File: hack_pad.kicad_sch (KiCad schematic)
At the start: 407 parts, among them J1 Barrel_Jack_Switch, Q1 IRLZ44N, Q2 IRF9540N, Q3 IRF9540N, Q4 IRLZ44N, SW1 SW_Push, SW10 SW_Push, SW100 SW_Push, SW11 SW_Push, SW12 SW_Push, SW13 SW_Push, SW14 SW_Push, SW15 SW_Push, SW16 SW_Push, SW17 SW_Push, SW18 SW_Push, SW19 SW_Push, SW2 SW_Push, SW20 SW_Push, SW21 SW_Push, SW22 SW_Push, SW23 SW_Push, SW24 SW_Push, SW25 SW_Push, SW26 SW_Push, SW27 SW_Push, SW28 SW_Push, SW29 SW_Push, SW3 SW_Push, SW30 SW_Push, SW31 SW_Push, SW32 SW_Push, SW33 SW_Push, SW34 SW_Push, SW35 SW_Push, SW36 SW_Push, SW37 SW_Push, SW38 SW_Push, SW39 SW_Push, SW4 SW_Push, SW40 SW_Push, SW41 SW_Push, SW42 SW_Push, SW43 SW_Push, SW44 SW_Push, SW45 SW_Push, SW46 SW_Push, SW47 SW_Push, SW48 SW_Push, SW49 SW_Push, SW5 SW_Push, SW50 SW_Push, SW51 SW_Push, SW52 SW_Push, SW53 SW_Push, SW54 SW_Push, SW55 SW_Push, SW56 SW_Push, SW57 SW_Push, SW58 SW_Push, SW59 SW_Push, SW6 SW_Push, SW60 SW_Push, SW61 SW_Push, SW62 SW_Push, SW63 SW_Push, SW64 SW_Push, SW65 SW_Push, SW66 SW_Push, SW67 SW_Push, SW68 SW_Push, SW69 SW_Push, SW7 SW_Push, SW70 SW_Push, SW71 SW_Push, SW72 SW_Push, SW73 SW_Push, SW74 SW_Push, SW75 SW_Push, SW76 SW_Push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

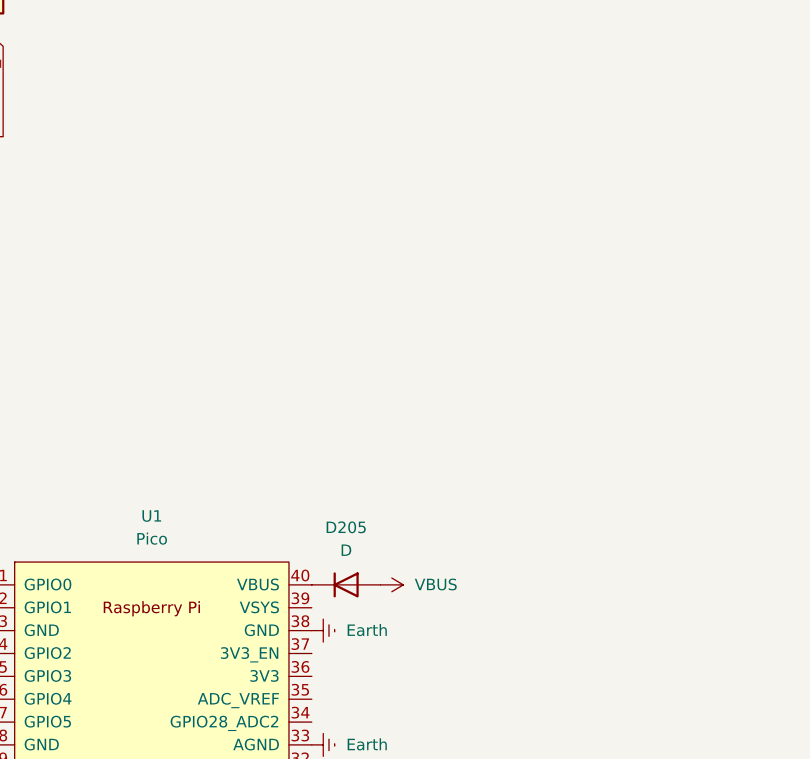
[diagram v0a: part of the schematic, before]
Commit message: Add initial journal entries and PCB lock file
- Created a journal.md to document the progress of the first PCB project, including details about the design, components, and layout.
- Added images of the PCB layout and components such as the RPI Pico and OLED.
- Introduced a lock file for the schematic to track user information.
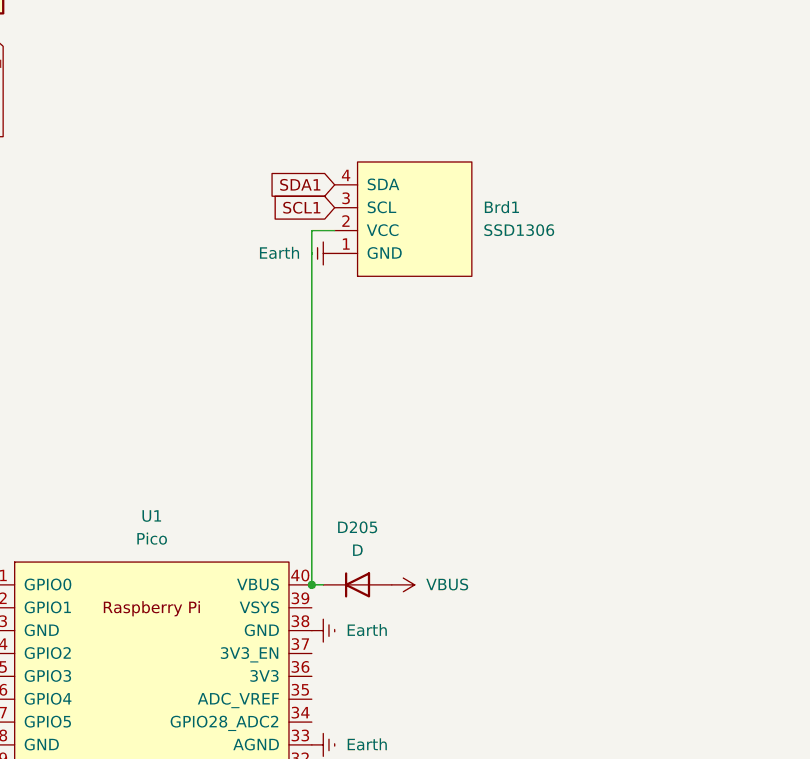
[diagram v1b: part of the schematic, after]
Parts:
- added Brd1: SSD1306, Display:OLED-128O064D, symbol SSD1306-0.91_OLED:SSD1306
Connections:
- net Earth: now also Brd1.1 (GND)
- net SCL1: now also Brd1.3 (SCL)
- net SDA1: now also Brd1.4 (SDA)
- net at D205.1 (K), U1.40 (VBUS): now also Brd1.2 (VCC)
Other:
- moved on the sheet: D205
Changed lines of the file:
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@@
 	)
 	(junction
+		(at 422.91 99.06)
+		(diameter 0)
+		(color 0 0 0 0)
+	)
+	(junction
 		(at 294.64 172.72)
 		(diameter 0)
@@
 	(wire
 		(pts
+			(xy 422.91 59.69) (xy 425.45 59.69)
+		)
+		(stroke
+			(width 0)
+			(type default)
+		)
+	)
+	(wire
+		(pts
 			(xy 76.2 190.5) (xy 91.44 190.5)
 		)
@@
 	(wire
 		(pts
+			(xy 424.18 99.06) (xy 422.91 99.06)
+		)
+		(stroke
+			(width 0)
+			(type default)
+		)
+	)
+	(wire
+		(pts
 			(xy 152.4 172.72) (xy 167.64 172.72)
 		)
@@
 	(wire
 		(pts
+			(xy 422.91 99.06) (xy 422.91 59.69)
+		)
+		(stroke
+			(width 0)
+			(type default)
+		)
+	)
+	(wire
+		(pts
 			(xy 157.48 111.76) (xy 157.48 129.54)
 		)
@@
 		)
 	)
+	(global_label "SCL1"
+		(shape input)
+		(at 425.45 57.15 180)
+		(fields_autoplaced yes)
+		(effects
+			(font
+				(size 1.27 1.27)
+			)
+			(justify right)
+		)
+		(property "Intersheetrefs" "${INTERSHEET_REFS}"
+			(at 417.7477 57.15 0)
+			(effects
+				(font
+					(size 1.27 1.27)
+				)
+				(justify right)
+				(hide yes)
+			)
+		)
+	)
+	(global_label "SDA1"
+		(shape input)
+		(at 425.45 54.61 180)
+		(fields_autoplaced yes)
+		(effects
+			(font
+				(size 1.27 1.27)
+			)
+			(justify right)
+		)
+		(property "Intersheetrefs" "${INTERSHEET_REFS}"
+			(at 417.6872 54.61 0)
+			(effects
+				(font
+					(size 1.27 1.27)
+				)
+				(justify right)
+				(hide yes)
+			)
+		)
+	)
 	(global_label "SDA1"
 		(shape input)
@@
 	(symbol
 		(lib_id "Device:D")
-		(at 426.72 99.06 0)
+		(at 427.99 99.06 0)
 		(unit 1)
 		(exclude_from_sim no)
@@
 		(fields_autoplaced yes)
 		(property "Reference" "D205"
-			(at 426.72 92.71 0)
+			(at 427.99 92.71 0)
 			(effects
 				(font
@@
 		)
 		(property "Value" "D"
-			(at 426.72 95.25 0)
+			(at 427.99 95.25 0)
 			(effects
 				(font
@@
 		)
 		(property "Footprint" "Diode_SMD:D_SMA_Handsoldering"
-			(at 426.72 99.06 0)
+			(at 427.99 99.06 0)
 			(effects
 				(font
@@
 		)
 		(property "Datasheet" "~"
-			(at 426.72 99.06 0)
+			(at 427.99 99.06 0)
 			(effects
 				(font
@@
 		)
 		(property "Description" "Diode"
-			(at 426.72 99.06 0)
+			(at 427.99 99.06 0)
 			(effects
 				(font
@@
 		)
 		(property "Sim.Device" "D"
-			(at 426.72 99.06 0)
+			(at 427.99 99.06 0)
 			(effects
 				(font
@@
 		)
 		(property "Sim.Pins" "1=K 2=A"
-			(at 426.72 99.06 0)
+			(at 427.99 99.06 0)
 			(effects
 				(font
@@
 	)
 	(symbol
+		(lib_id "SSD1306-0.91_OLED:SSD1306")
+		(at 434.34 58.42 90)
+		(unit 1)
+		(exclude_from_sim no)
+		(in_bom yes)
+		(on_board yes)
+		(dnp no)
+		(fields_autoplaced yes)
+		(property "Reference" "Brd1"
+			(at 441.96 57.1499 90)
+			(effects
+				(font
+					(size 1.27 1.27)
+				)
+				(justify right)
+			)
+		)
+		(property "Value" "SSD1306"
+			(at 441.96 59.6899 90)
+			(effects
+				(font
+					(size 1.27 1.27)
+				)
+				(justify right)
+			)
+		)
+		(property "Footprint" "Display:OLED-128O064D"
+			(at 427.99 58.42 0)
+			(effects
+				(font
+					(size 1.27 1.27)
+				)
+				(hide yes)
+			)
+		)
+		(property "Datasheet" ""
+			(at 427.99 58.42 0)
+			(effects
+				(font
+					(size 1.27 1.27)
+				)
+				(hide yes)
+			)
+		)
+		(property "Description" "SSD1306 OLED"
+			(at 434.34 58.42 0)
+			(effects
+				(font
+					(size 1.27 1.27)
+				)
+				(hide yes)
+			)
+		)
+		(pin "2"
+		)
+		(pin "3"
+		)
+		(pin "4"
+		)
+		(pin "1"
+		)
+		(instances
+			(project ""
+				(path "/d4b0ca01-3fca-43e7-acf5-9c62f788d69d"
+					(reference "Brd1")
+					(unit 1)
+				)
+			)
+		)
+	)
+	(symbol
 		(lib_id "LED:SK6812MINI")
 		(at 237.49 210.82 0)
@@
 	(symbol
 		(lib_id "power:Earth")
+		(at 425.45 62.23 270)
+		(unit 1)
+		(exclude_from_sim no)
+		(in_bom yes)
+		(on_board yes)
+		(dnp no)
+		(fields_autoplaced yes)
+		(property "Reference" "#PWR0212"
+			(at 419.1 62.23 0)
+			(effects
+				(font
+					(size 1.27 1.27)
+				)
+				(hide yes)
+			)
+		)
+		(property "Value" "Earth"
+			(at 421.64 62.2299 90)
+			(effects
+				(font
+					(size 1.27 1.27)
+				)
+				(justify right)
+			)
+		)
+		(property "Footprint" ""
+			(at 425.45 62.23 0)
+			(effects
+				(font
+					(size 1.27 1.27)
+				)
+				(hide yes)
+			)
+		)
+		(property "Datasheet" "~"
+			(at 425.45 62.23 0)
+			(effects
+				(font
+					(size 1.27 1.27)
+				)
+				(hide yes)
+			)
+		)
+		(property "Description" "Power symbol creates a global label with name \"Earth\""
+			(at 425.45 62.23 0)
+			(effects
+				(font
+					(size 1.27 1.27)
+				)
+				(hide yes)
+			)
+		)
+		(pin "1"
+		)
+		(instances
+			(project "hack_pad"
+				(path "/d4b0ca01-3fca-43e7-acf5-9c62f788d69d"
+					(reference "#PWR0212")
+					(unit 1)
+				)
+			)
+		)
+	)
+	(symbol
+		(lib_id "power:Earth")
 		(at 256.54 25.4 180)
 		(unit 1)
@@
 	(symbol
 		(lib_id "power:VBUS")
-		(at 430.53 99.06 270)
+		(at 431.8 99.06 270)
 		(unit 1)
 		(exclude_from_sim no)
@@
 		(fields_autoplaced yes)
 		(property "Reference" "#PWR0204"
-			(at 426.72 99.06 0)
+			(at 427.99 99.06 0)
 			(effects
 				(font
@@
 		)
 		(property "Value" "VBUS"
-			(at 434.34 99.0599 90)
+			(at 435.61 99.0599 90)
 			(effects
 				(font
@@
 		)
 		(property "Footprint" ""
-			(at 430.53 99.06 0)
+			(at 431.8 99.06 0)
 			(effects
 				(font
@@
 		)
 		(property "Datasheet" ""
-			(at 430.53 99.06 0)
+			(at 431.8 99.06 0)
 			(effects
 				(font
@@
 		)
 		(property "Description" "Power symbol creates a global label with name \"VBUS\""
-			(at 430.53 99.06 0)
+			(at 431.8 99.06 0)
 			(effects
 				(font

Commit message: Add lock file for hack_pad PCB with hostname and username information
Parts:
- Brd1: footprint Display:OLED-128O064D -> footprints:SSD1306-0.91-OLED-4pin-128x32
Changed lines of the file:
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@@
 			)
 		)
-		(property "Footprint" "Display:OLED-128O064D"
+		(property "Footprint" "footprints:SSD1306-0.91-OLED-4pin-128x32"
 			(at 427.99 58.42 0)
 			(effects
